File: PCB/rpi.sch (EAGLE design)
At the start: 63 parts, among them IC2 MC1541TO, IC4 MEGA16-A, X1 2526-

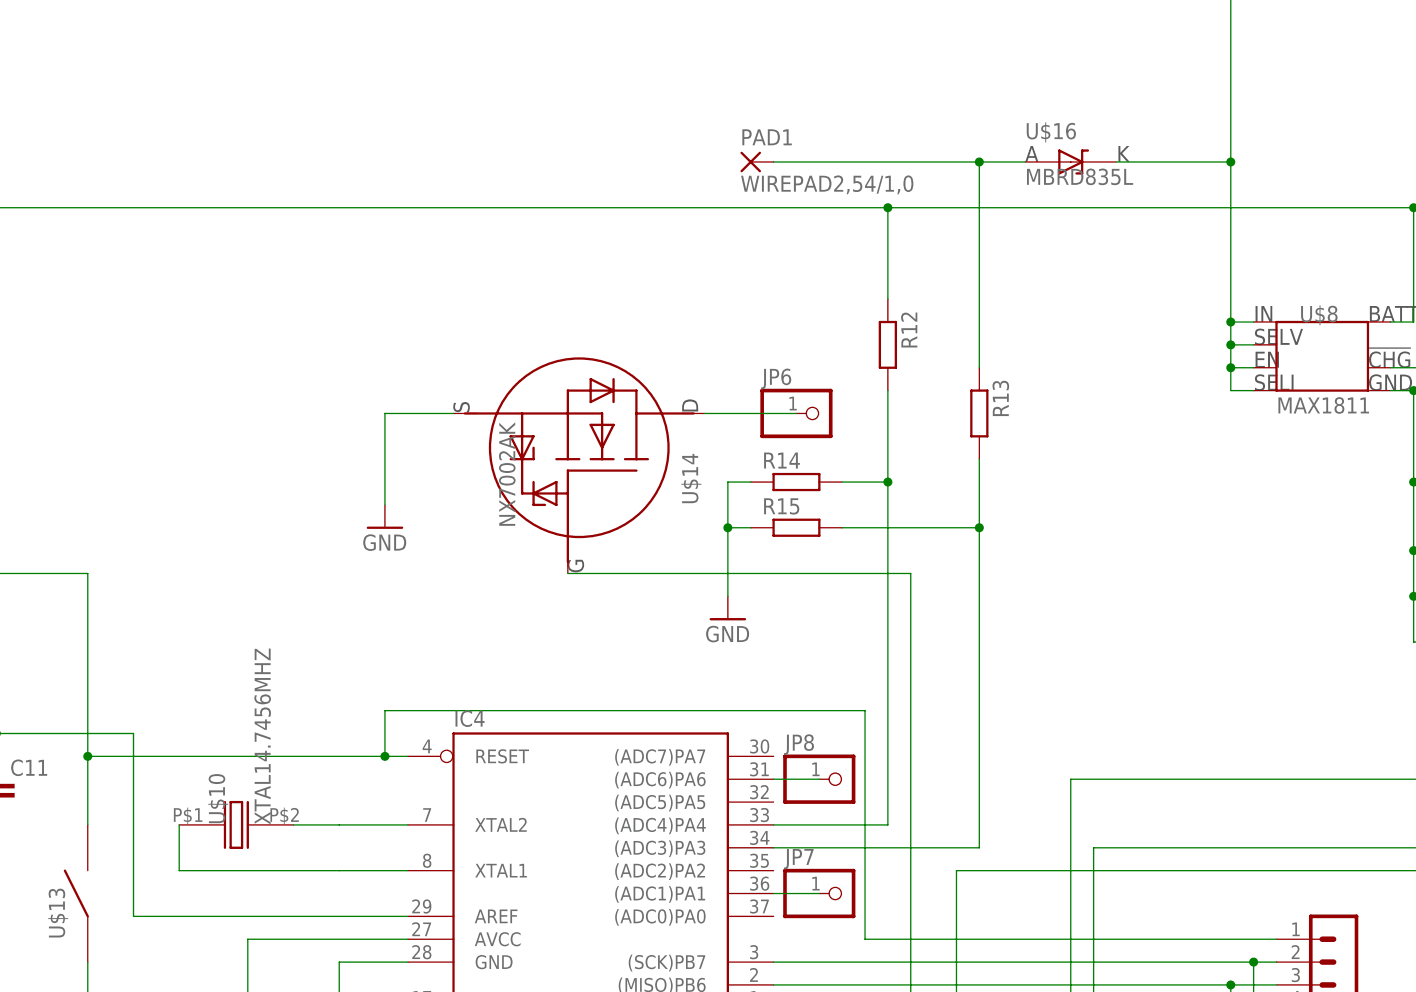
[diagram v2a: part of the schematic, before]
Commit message: On branch master 	modified:   PCB/eagle.epf 	modified:   PCB/rpi.brd 	modified:   PCB/rpi.sch
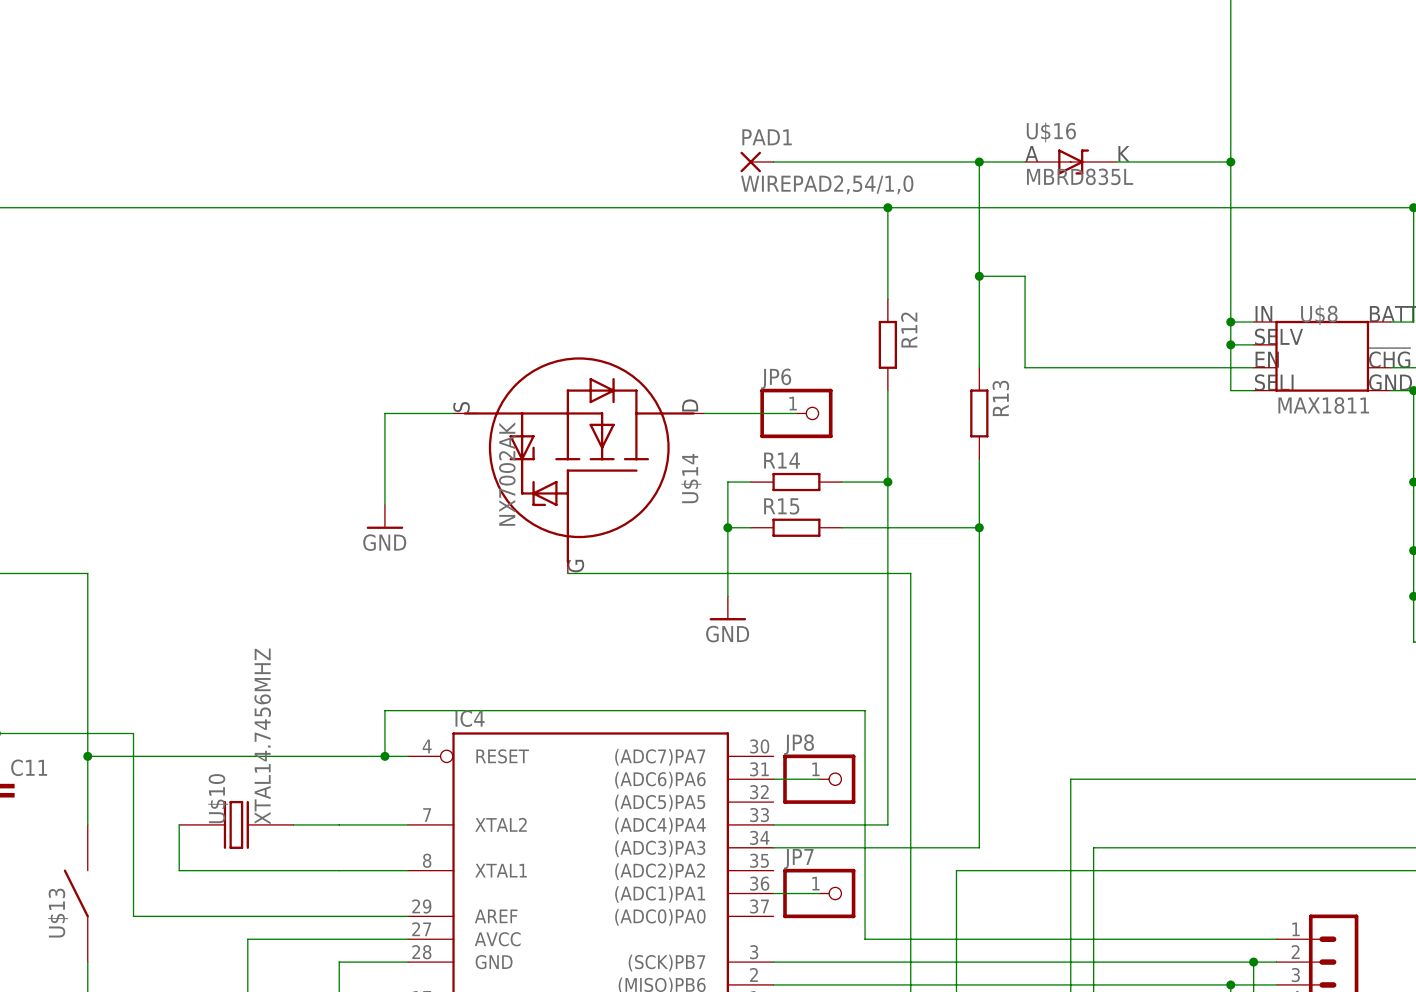
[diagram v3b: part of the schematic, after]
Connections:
- net +5V: no longer U$8.EN
- net N$17: now also U$8.EN
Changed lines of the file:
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@@
 <pinref part="U$8" gate="G$1" pin="SELI"/>
 <wire x1="200.66" y1="195.58" x2="198.12" y2="195.58" width="0.1524" layer="91"/>
-<wire x1="198.12" y1="195.58" x2="198.12" y2="198.12" width="0.1524" layer="91"/>
 <junction x="198.12" y="203.2"/>
-<wire x1="198.12" y1="198.12" x2="198.12" y2="200.66" width="0.1524" layer="91"/>
+<wire x1="198.12" y1="195.58" x2="198.12" y2="200.66" width="0.1524" layer="91"/>
 <wire x1="198.12" y1="200.66" x2="198.12" y2="203.2" width="0.1524" layer="91"/>
 <wire x1="198.12" y1="203.2" x2="198.12" y2="220.98" width="0.1524" layer="91"/>
@@
 <pinref part="U$11" gate="G$1" pin="S"/>
 <wire x1="373.38" y1="200.66" x2="365.76" y2="200.66" width="0.1524" layer="91"/>
-<pinref part="U$8" gate="G$1" pin="EN"/>
-<wire x1="200.66" y1="198.12" x2="198.12" y2="198.12" width="0.1524" layer="91"/>
-<junction x="198.12" y="198.12"/>
 <pinref part="U$1" gate="G$1" pin="DRV"/>
 <pinref part="C3" gate="G$1" pin="1"/>
@@
 <pinref part="R13" gate="G$1" pin="1"/>
 <wire x1="170.18" y1="220.98" x2="175.26" y2="220.98" width="0.1524" layer="91"/>
-<wire x1="170.18" y1="198.12" x2="170.18" y2="220.98" width="0.1524" layer="91"/>
+<wire x1="170.18" y1="198.12" x2="170.18" y2="208.28" width="0.1524" layer="91"/>
 <junction x="170.18" y="220.98"/>
-</segment>
-</net>
+<pinref part="U$8" gate="G$1" pin="EN"/>
+<wire x1="170.18" y1="208.28" x2="170.18" y2="220.98" width="0.1524" layer="91"/>
+<wire x1="200.66" y1="198.12" x2="175.26" y2="198.12" width="0.1524" layer="91"/>
+<wire x1="175.26" y1="198.12" x2="175.26" y2="208.28" width="0.1524" layer="91"/>
+<wire x1="175.26" y1="208.28" x2="170.18" y2="208.28" width="0.1524" layer="91"/>
+<junction x="170.18" y="208.28"/>
+</segment>
+</net>

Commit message: On branch master 	modified:   PCB/eagle.epf 	modified:   PCB/rpi.brd 	modified:   PCB/rpi.sch 	modified:   RaspberryPI-shutdown/RaspberryPI-shutdown.pro 	modified:   RaspberryPI/RaspberryPI.pro
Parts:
- JP1: device con-lstb:MA04-1 -> tablet:MA04-1
- SV1: device con-lstb:MA04-2 -> tablet:MA04-2
- X1: device con-3m:2526- -> tablet:2526-
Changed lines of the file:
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@@
 <grid distance="0.1" unitdist="inch" unit="inch" style="lines" multiple="1" display="no" altdistance="0.01" altunitdist="inch" altunit="inch"/>
 <layers>
-<layer number="1" name="Top" color="4" fill="1" visible="yes" active="no"/>
-<layer number="16" name="Bottom" color="1" fill="1" visible="yes" active="no"/>
-<layer number="17" name="Pads" color="2" fill="1" visible="yes" active="no"/>
-<layer number="18" name="Vias" color="2" fill="1" visible="yes" active="no"/>
-<layer number="19" name="Unrouted" color="6" fill="1" visible="yes" active="no"/>
-<layer number="20" name="Dimension" color="15" fill="1" visible="yes" active="no"/>
-<layer number="21" name="tPlace" color="7" fill="1" visible="yes" active="no"/>
-<layer number="22" name="bPlace" color="7" fill="1" visible="yes" active="no"/>
-<layer number="23" name="tOrigins" color="15" fill="1" visible="yes" active="no"/>
-<layer number="24" name="bOrigins" color="15" fill="1" visible="yes" active="no"/>
-<layer number="25" name="tNames" color="7" fill="1" visible="yes" active="no"/>
-<layer number="26" name="bNames" color="7" fill="1" visible="yes" active="no"/>
-<layer number="27" name="tValues" color="7" fill="1" visible="yes" active="no"/>
-<layer number="28" name="bValues" color="7" fill="1" visible="yes" active="no"/>
+<layer number="1" name="Top" color="4" fill="1" visible="no" active="no"/>
+<layer number="16" name="Bottom" color="1" fill="1" visible="no" active="no"/>
+<layer number="17" name="Pads" color="2" fill="1" visible="no" active="no"/>
+<layer number="18" name="Vias" color="2" fill="1" visible="no" active="no"/>
+<layer number="19" name="Unrouted" color="6" fill="1" visible="no" active="no"/>
+<layer number="20" name="Dimension" color="15" fill="1" visible="no" active="no"/>
+<layer number="21" name="tPlace" color="7" fill="1" visible="no" active="no"/>
+<layer number="22" name="bPlace" color="7" fill="1" visible="no" active="no"/>
+<layer number="23" name="tOrigins" color="15" fill="1" visible="no" active="no"/>
+<layer number="24" name="bOrigins" color="15" fill="1" visible="no" active="no"/>
+<layer number="25" name="tNames" color="7" fill="1" visible="no" active="no"/>
+<layer number="26" name="bNames" color="7" fill="1" visible="no" active="no"/>
+<layer number="27" name="tValues" color="7" fill="1" visible="no" active="no"/>
+<layer number="28" name="bValues" color="7" fill="1" visible="no" active="no"/>
 <layer number="29" name="tStop" color="7" fill="3" visible="no" active="no"/>
 <layer number="30" name="bStop" color="7" fill="6" visible="no" active="no"/>
@@
 <layer number="35" name="tGlue" color="7" fill="4" visible="no" active="no"/>
 <layer number="36" name="bGlue" color="7" fill="5" visible="no" active="no"/>
-<layer number="37" name="tTest" color="7" fill="1" visible="yes" active="no"/>
-<layer number="38" name="bTest" color="7" fill="1" visible="yes" active="no"/>
+<layer number="37" name="tTest" color="7" fill="1" visible="no" active="no"/>
+<layer number="38" name="bTest" color="7" fill="1" visible="no" active="no"/>
 <layer number="39" name="tKeepout" color="4" fill="11" visible="no" active="no"/>
 <layer number="40" name="bKeepout" color="1" fill="11" visible="no" active="no"/>
@@
 <layer number="44" name="Drills" color="7" fill="1" visible="no" active="no"/>
 <layer number="45" name="Holes" color="7" fill="1" visible="no" active="no"/>
-<layer number="46" name="Milling" color="3" fill="1" visible="yes" active="no"/>
-<layer number="47" name="Measures" color="7" fill="1" visible="yes" active="no"/>
-<layer number="48" name="Document" color="7" fill="1" visible="yes" active="no"/>
-<layer number="49" name="Reference" color="7" fill="1" visible="yes" active="no"/>
-<layer number="51" name="tDocu" color="7" fill="1" visible="yes" active="no"/>
-<layer number="52" name="bDocu" color="7" fill="1" visible="yes" active="no"/>
+<layer number="46" name="Milling" color="3" fill="1" visible="no" active="no"/>
+<layer number="47" name="Measures" color="7" fill="1" visible="no" active="no"/>
+<layer number="48" name="Document" color="7" fill="1" visible="no" active="no"/>
+<layer number="49" name="Reference" color="7" fill="1" visible="no" active="no"/>
+<layer number="51" name="tDocu" color="7" fill="1" visible="no" active="no"/>
+<layer number="52" name="bDocu" color="7" fill="1" visible="no" active="no"/>
 <layer number="91" name="Nets" color="2" fill="1" visible="yes" active="yes"/>
 <layer number="92" name="Busses" color="1" fill="1" visible="yes" active="yes"/>
@@
 <part name="R3" library="resistor" deviceset="R-EU_" device="R1206" value="3000"/>
 <part name="R4" library="resistor" deviceset="R-EU_" device="R1206" value="2000"/>
-<part name="JP1" library="con-lstb" deviceset="MA04-1" device=""/>
+<part name="JP1" library="tablet" deviceset="MA04-1" device=""/>
 <part name="GND4" library="supply1" deviceset="GND" device=""/>
-<part name="X1" library="con-3m" deviceset="2526-" device=""/>
-<part name="SV1" library="con-lstb" deviceset="MA04-2" device=""/>
+<part name="X1" library="tablet" deviceset="2526-" device=""/>
+<part name="SV1" library="tablet" deviceset="MA04-2" device=""/>
 <part name="U$2" library="tablet" deviceset="NX7002AK" device=""/>
 <part name="U$8" library="tablet" deviceset="MAX1811" device=""/>
